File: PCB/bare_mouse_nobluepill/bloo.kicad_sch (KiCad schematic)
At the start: 105 parts, among them J1 Serial Debug Header, J10 Conn_01x06_Female, J2 SWD Header, J4 Conn_ARM_JTAG_SWD_10, J5 SWD Header, M1 M1_Conn_Alt, M2 M2_Conn_Alt, Q0 TEFT4300, Q1 TEFT4300, Q10 Q_NMOS_GSD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

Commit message: Created second kicad directory for version of micromouse without bluepill (using solely STM chip). Updated BOM accordingly and updated schematic for said file
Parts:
- removed U1: YAAJ_BluePill_SWD_Breakout, MM_Library:STM32F103, symbol YAAJ_BluePill_SWD_Breakout:YAAJ_BluePill_SWD_Breakout
- added C22, C23, C24, C26: 0.1uF, Capacitor_SMD:C_1206_3216Metric_Pad1.33x1.80mm_HandSolder, symbol Device:C
- added C27: 10uF, Capacitor_SMD:C_1206_3216Metric_Pad1.33x1.80mm_HandSolder, symbol Device:C
- added C28: 1uF, Capacitor_SMD:C_1206_3216Metric_Pad1.33x1.80mm_HandSolder, symbol Device:C
- added C29: 0.01uF, Capacitor_SMD:C_1206_3216Metric_Pad1.33x1.80mm_HandSolder, symbol Device:C
- added R10, R25: 10K, Resistor_SMD:R_1206_3216Metric_Pad1.30x1.75mm_HandSolder, symbol Device:R
- added U7: STM32F103C8Tx, Package_QFP:LQFP-48_7x7mm_P0.5mm, symbol MCU_ST_STM32F1:STM32F103C8Tx
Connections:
- net +3.3VA: now also C28.1, C29.1, U7.9 (VDDA)
- net +3V3: now also C22.1, C23.1, C24.1, C26.1, C27.1, U7.1 (VBAT), U7.24 (VDD), U7.36 (VDD), U7.48 (VDD)
- net AGND: now also C28.2, C29.2
- net BLE_STATE: now also U7.10 (PA0)
- net BUTTON: now also U7.40 (PB4)
- net BUTTON_2: now also U7.3 (PC14)
- net BUTTON_3: now also U7.46 (PB9)
- net BUZZER: now also U7.45 (PB8)
- net EMIT_1: now also U7.25 (PB12)
- net EMIT_2: now also U7.22 (PB11)
- net EMIT_3: now also U7.21 (PB10)
- net EMIT_4: now also U7.41 (PB5)
- net GND: now also C22.2, C23.2, C24.2, C26.2, C27.2, R10.1, R25.1, U7.23 (VSS), U7.35 (VSS), U7.47 (VSS), U7.8 (VSSA)
- net LED_BLUE: now also U7.33 (PA12)
- net LED_GREEN: now also U7.38 (PA15)
- net LED_RED: now also U7.32 (PA11)
- net M1_BACK: now also U7.27 (PB14)
- net M1_ENC_A: now also U7.16 (PA6)
- net M1_ENC_B: now also U7.17 (PA7)
- net M1_FWD: now also U7.29 (PA8)
- net M1_SPD: now also U7.13 (PA3)
- net M2_BACK: now also U7.28 (PB15)
- net M2_ENC_A: now also U7.43 (PB7)
- net M2_ENC_B: now also U7.42 (PB6)
- net M2_FWD: now also U7.26 (PB13)
- net M2_SPD: now also U7.12 (PA2)
- net RECEIV_1: now also U7.19 (PB1)
- net RECEIV_2: now also U7.18 (PB0)
- net RECEIV_3: now also U7.15 (PA5)
- net RECEIV_4: now also U7.14 (PA4)
- net RST: now also U7.7 (NRST)
- net SWDCLK: now also U7.37 (PA14)
- net SWDIO: now also U7.34 (PA13)
- net SWO: now also U7.39 (PB3)
- net USART1_RX: now also U7.31 (PA10)
- net USART1_TX: now also U7.30 (PA9)
- net V_METER: now also U7.11 (PA1)
- new net: R25.2, U7.20 (PB2)
- new net BOOT0: R10.2, U7.44 (BOOT0)
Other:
- note added: "Pins for external oscillator"
- moved on the sheet: C6, C8, FB3, FB4, J1, J10

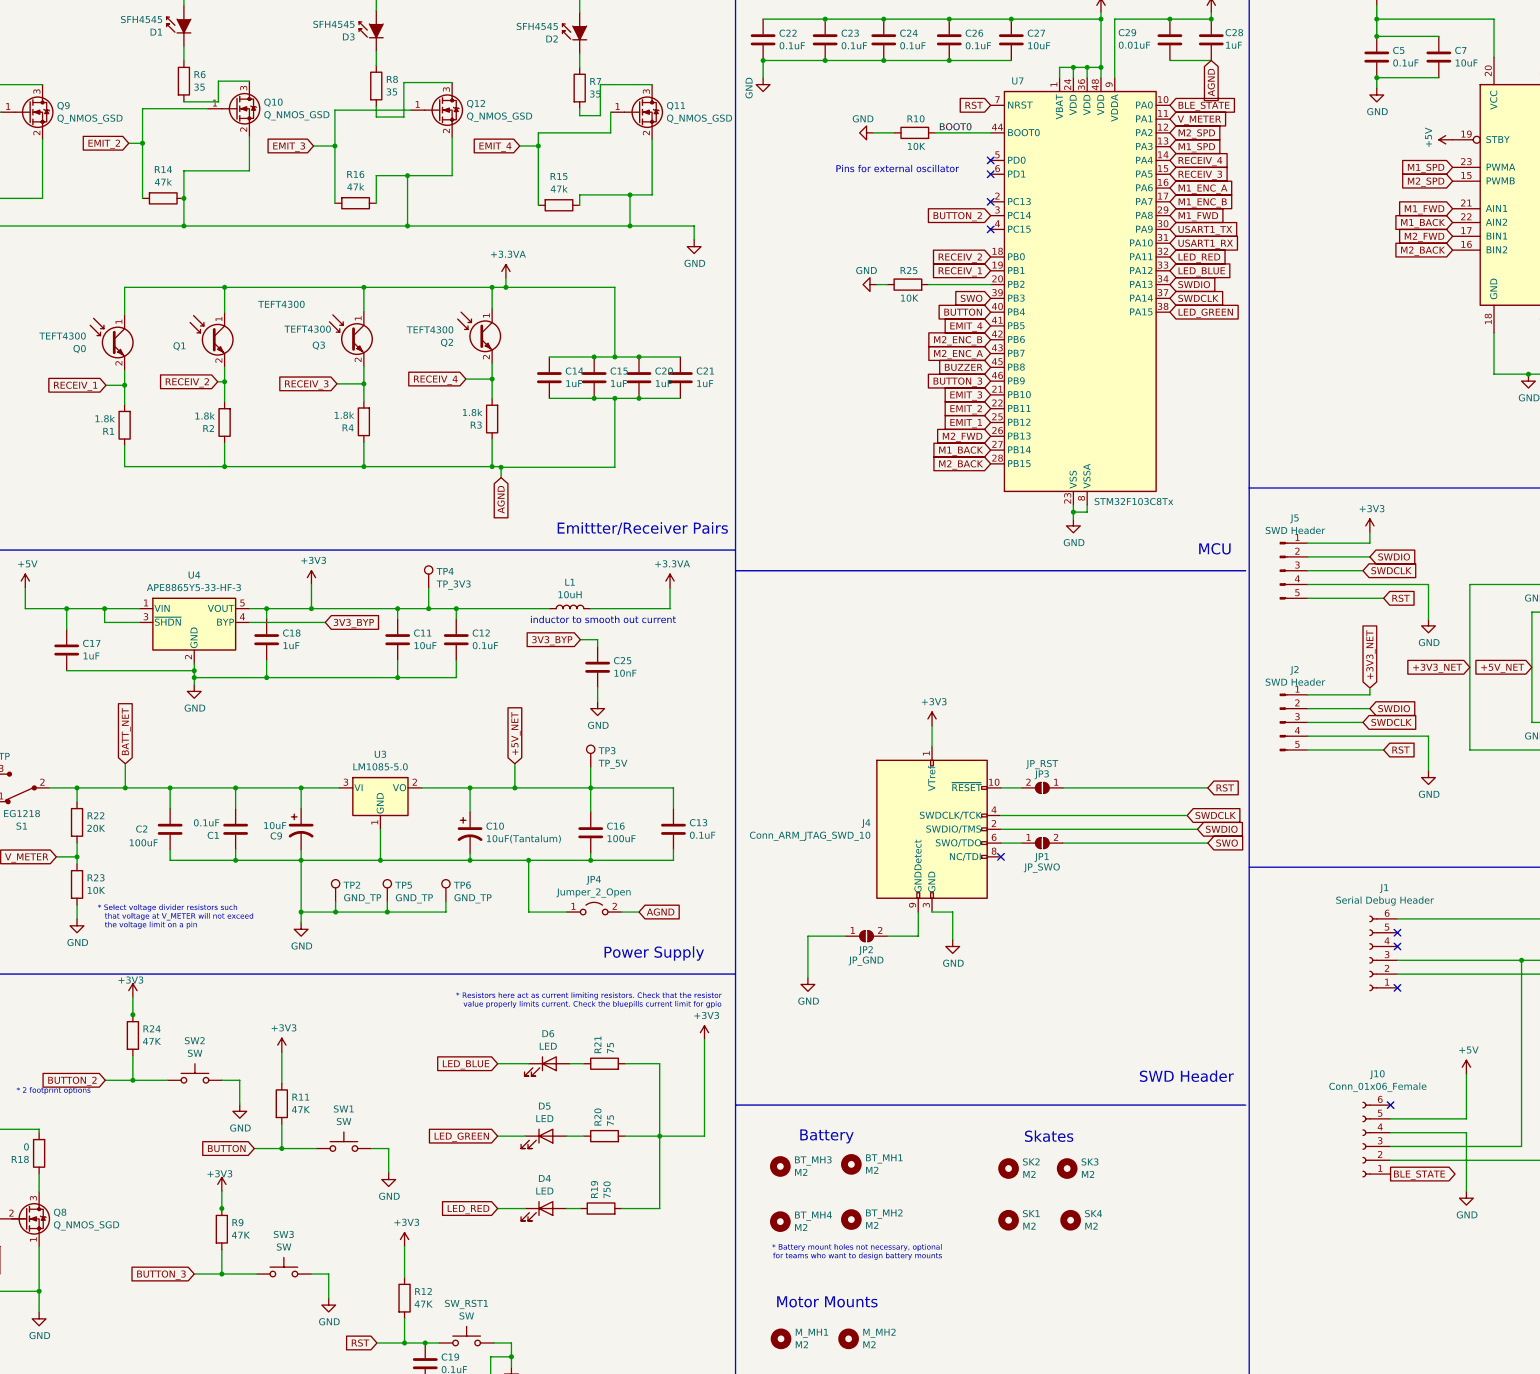
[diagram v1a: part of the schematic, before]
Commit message: Reviewed and updated schematics accordingly, updated BOM, created PCB Design Notes
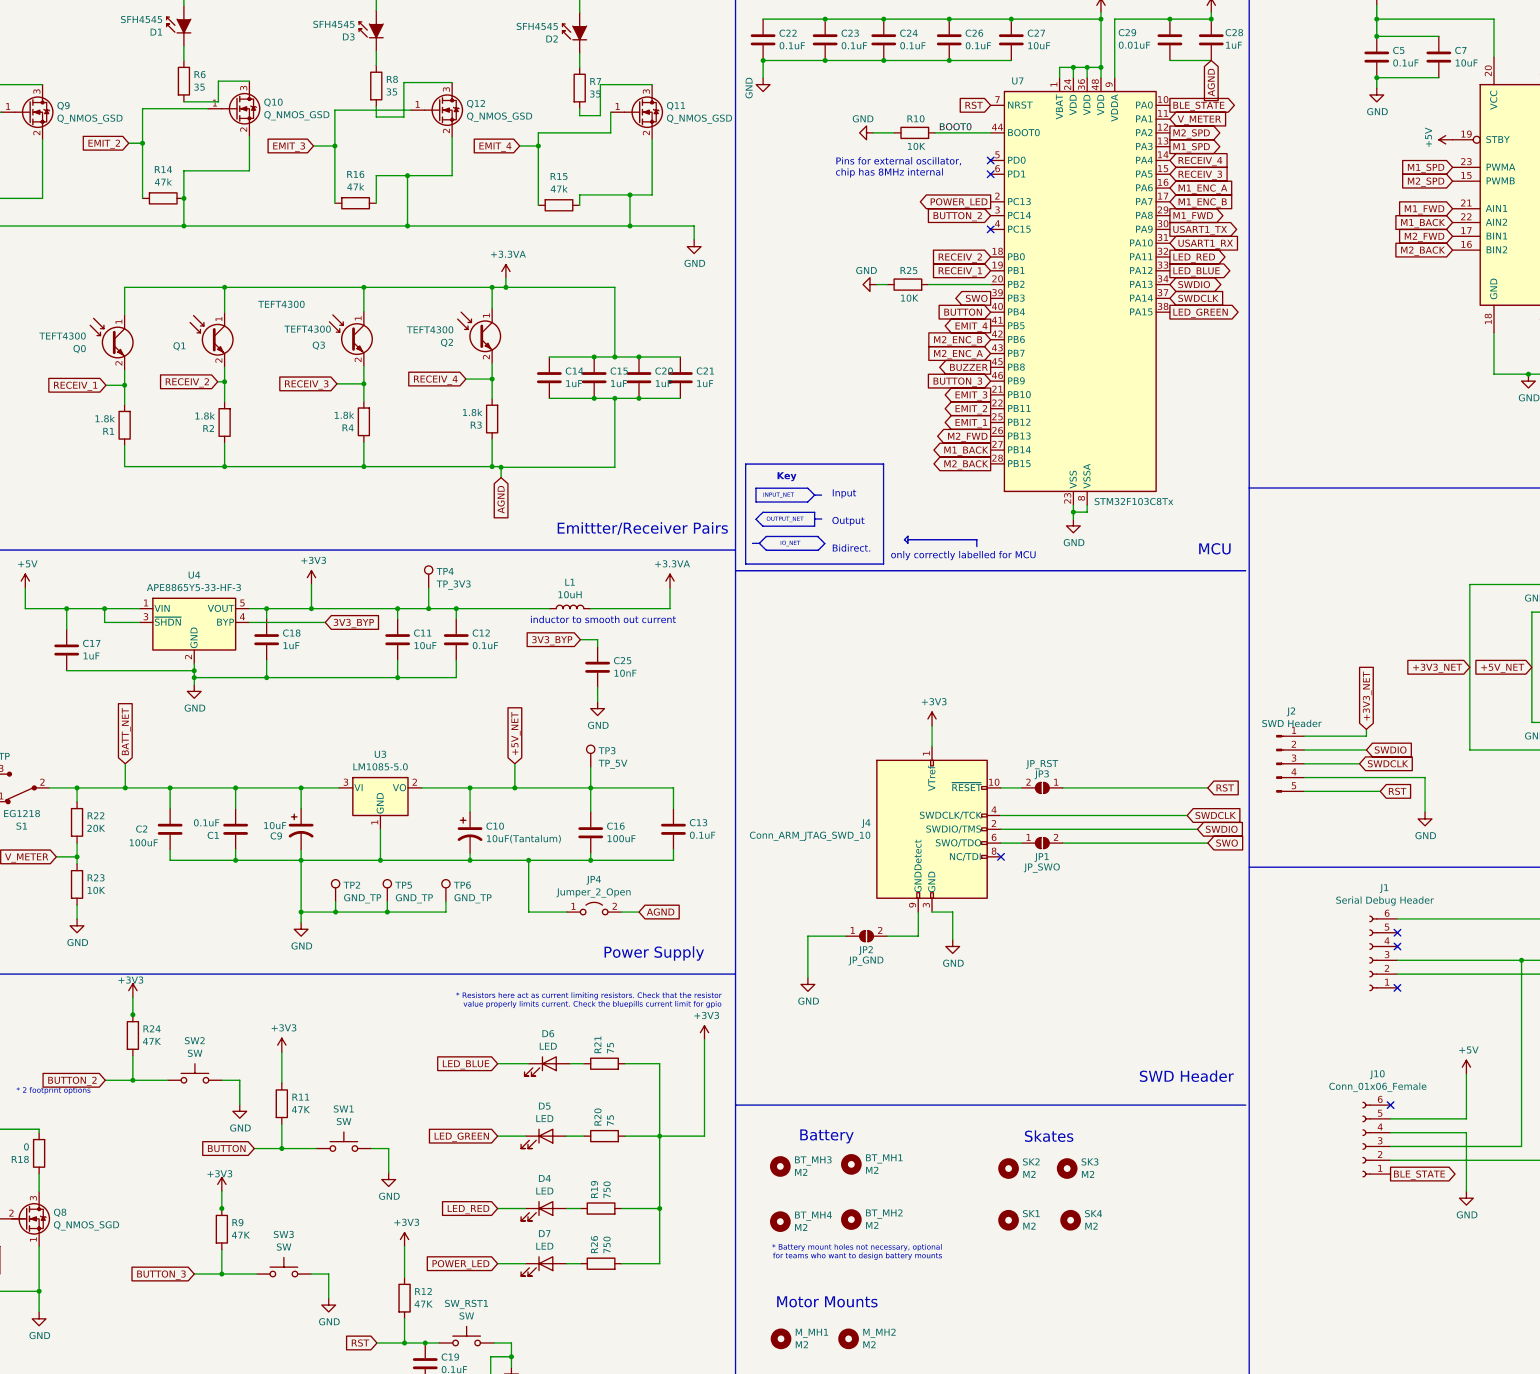
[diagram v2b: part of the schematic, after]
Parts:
- removed J5: SWD Header, Connector_PinHeader_2.54mm:PinHeader_1x05_P2.54mm_Vertical, symbol Connector:Conn_01x05_Male
- added D7: LED, LED_SMD:LED_0805_2012Metric_Pad1.15x1.40mm_HandSolder, symbol bloo-rescue:LED-Device-mouse_v2-rescue
- added R26: 750, Resistor_SMD:R_1206_3216Metric_Pad1.30x1.75mm_HandSolder, symbol bloo-rescue:R-Device-mouse_v2-rescue
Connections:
- net +3V3: now also R26.2
- net POWER_LED: now reaches U7.2 (PC13)
- net POWER_LED: now also D7.1 (K)
- new net: D7.2 (A), R26.1
- no-connect marks 9 -> 8
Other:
- note added: "Bidirect."
- note added: "INPUT_NET"
- note added: "IO_NET"
- note added: "Input"
- note added: "Key"
- note added: "OUTPUT_NET"
- note added: "Output"
- note added: "Pins for external oscillator, chip has 8MHz internal"
- note added: "only correctly labelled for MCU"
- note removed: "* Select voltage divider resistors such that voltage at V_METER will not exceed the voltage limit on a pin"
- note removed: "Pins for external oscillator"
- moved on the sheet: J2
